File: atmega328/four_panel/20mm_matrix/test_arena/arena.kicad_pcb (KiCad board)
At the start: 2 copper layers, 260 x 50 mm, 35 parts, among them M1 VAL**, M2 VAL**, M3 VAL**, M4 VAL**, M5 VAL**, M6 VAL**, P1 CONN15, P10 CONN_2X2, P11 CONN_2X2, P12 CONN_2X2, P13 CONN_2X2, P14 CONN_2X2, P15 CONN_2X2, P16 CONN_2X2, P17 CONN_2X2, P18 CONN_2X2, P19 CONN_2X2, P2 CONN15, P20 CONN_2X2, P21 CONN_2X2, P22 CONN_20X2, P23 CONN_30X2, P24 CONN_2, P3 CONN15, P4 CONN15, P5 CONN15, P6 CONN15, P7 CONN_2X2, P8 CONN_2X2, P9 CONN_2X2

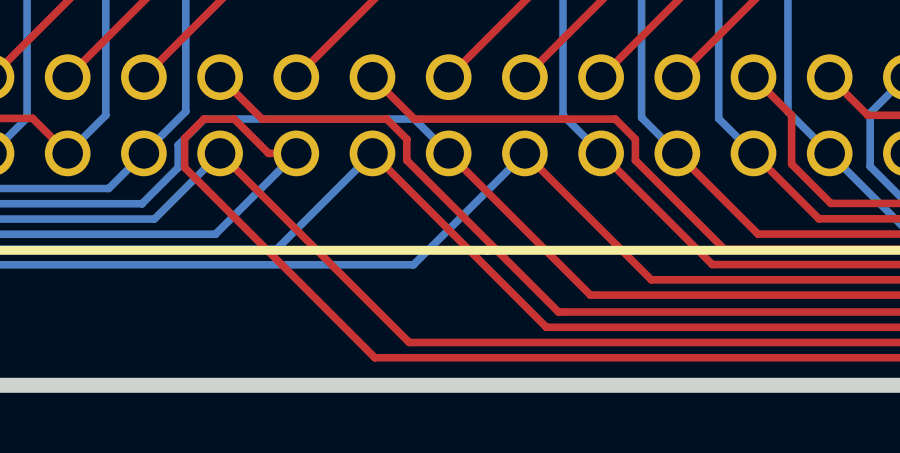
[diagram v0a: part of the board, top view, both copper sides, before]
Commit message: Fixed minor issues with test arenas and programmer pcbs.
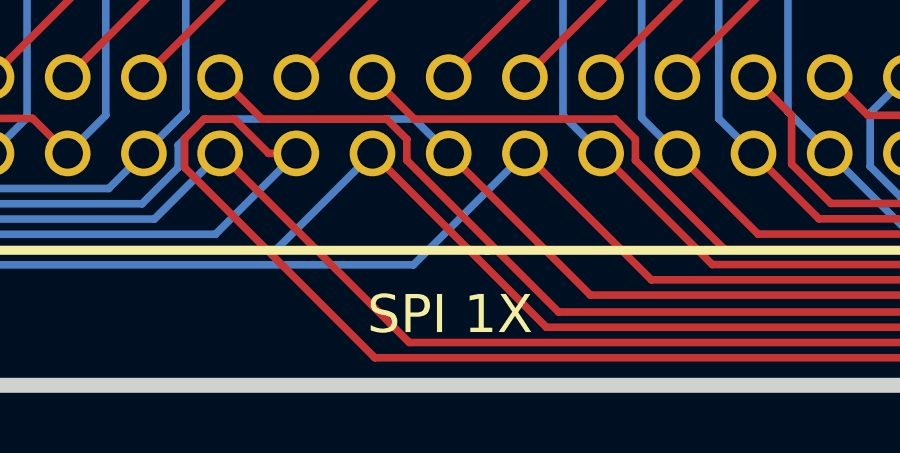
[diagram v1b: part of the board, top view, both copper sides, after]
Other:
- board text added: "SPI 1X"
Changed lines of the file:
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@@
     (links 189)
     (no_connects 0)
-    (area 0 0 0 0)
+    (area 39.749999 49.527499 311.349571 100.250001)
     (thickness 1.6)
     (drawings 53)
@@
     (visible_elements FFFFFF7F)
     (pcbplotparams
-      (layerselection 3178497)
-      (usegerberextensions true)
+      (layerselection 271613953)
+      (usegerberextensions false)
       (excludeedgelayer true)
       (linewidth 0.150000)
@@
       (outputformat 1)
       (mirror false)
-      (drillshape 1)
+      (drillshape 0)
       (scaleselection 1)
       (outputdirectory ""))
@@
     )
   )
+  (gr_text "SPI 1X" (at 115.7732 97.6376) (layer F.SilkS)
+    (effects (font (size 1.27 1.27) (thickness 0.254)))
+  )
   (gr_text "4x 20mm Atmega328 Test Arena v0.1\nwww.iorodeo.com" (at 292.989 77.343 90) (layer F.SilkS)
     (effects (font (size 1.27 1.27) (thickness 0.254)))
@@
     (effects (font (size 1.27 1.27) (thickness 0.254)))
   )
-  (gr_line (start 143 87) (end 197 87) (angle 90) (layer Dwgs.User) (width 0.2))
   (gr_line (start 300 50) (end 300 100) (angle 90) (layer Edge.Cuts) (width 0.5))
   (gr_line (start 40 100) (end 300 100) (angle 90) (layer Edge.Cuts) (width 0.5))

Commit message: Added 3rd spi header to test arenas. Third header has 6 spi buses w/ 5 common cs lines.
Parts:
- added P25: CONN_5X2, PIN_ARRAY_5x2, F.Cu at (109.8, 77.0)
- added P26: CONN_5X2, PIN_ARRAY_5x2, F.Cu at (149.9, 77.0)
- added P27: CONN_5X2, PIN_ARRAY_5x2, F.Cu at (190.1, 77.0)
- added P28: CONN_5X2, PIN_ARRAY_5x2, F.Cu at (230.2, 77.0)
- added P29: CONN_5X2, PIN_ARRAY_5x2, F.Cu at (270.2, 77.0)
- added P30: CONN_20X2, PIN_ARRAY_SHRD_20X2, F.Cu at (174.0, 89.0)
- moved P23 13.2 mm to (250.0, 89.0)
- moved P22 7.28 mm to (110.0, 89.0)
- moved P24 6.50 mm to (56.5, 86.2)
- moved P10 4.00 mm to (222.7, 66.0)
- moved P11 4.00 mm to (262.8, 66.0)
- moved P12 4.00 mm to (109.8, 66.0)
- moved P13 4.00 mm to (149.9, 66.0)
- moved P14 4.00 mm to (190.1, 66.0)
- moved P15 4.00 mm to (230.2, 66.0)
- moved P16 4.00 mm to (270.2, 66.0)
- moved P17 4.00 mm to (117.3, 66.0)
- moved P18 4.00 mm to (157.4, 66.0)
- moved P19 4.00 mm to (197.6, 66.0)
- moved P20 4.00 mm to (237.7, 66.0)
- moved P21 4.00 mm to (277.8, 66.0)
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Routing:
- net /CS4_0: track 184.6 -> 308.4 mm, vias 0 -> 1
- net /CS3_0: track 192.1 -> 299.7 mm, vias 0 -> 1
- net /CS5_0: track 210.2 -> 308.2 mm, vias 0 -> 3
- net /CS1_0: track 179.8 -> 277.0 mm, vias 0 -> 2
- net /CS2_0: track 188.1 -> 283.3 mm
- net /SCK_5: track 26.0 -> 120.4 mm, vias 0 -> 2
- net /MOSI_5: track 32.9 -> 125.3 mm
- net /MOSI_4: track 19.8 -> 109.1 mm
- net /SCK_4: track 19.1 -> 103.3 mm, vias 0 -> 1
- net /MISO_5: track 50.4 -> 132.8 mm, vias 0 -> 1
- net /MISO_4: track 36.4 -> 107.1 mm
- net /CS5_2: track 213.0 -> 282.8 mm, vias 2 -> 0
- net /CS5_3: track 146.4 -> 213.3 mm
- net /MOSI_0: track 293.5 -> 346.1 mm, vias 0 -> 2
- net /CS2_3: track 147.2 -> 198.7 mm, vias 1 -> 2
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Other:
- board text added: "CS-COMMON"
- board text added: "SPI 1X, CS-COMMON"
